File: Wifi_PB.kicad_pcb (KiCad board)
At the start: 2 copper layers, 100 x 49.7 mm, 208 parts, among them P1 CONN_01X02, P10 CONN_01X01, P12 CONN_01X04, P13 CONN_01X04, P14 CONN_01X04, P15 USB_MINI, P16 CONN_01X01, P17 CONN_01X01, P18 CONN_01X01, P19 CONN_01X01, P2 CONN_01X03, P3 CONN_01X03, P4 CONN_01X03, P5 CONN_01X03, P6 CONN_01X01, P7 CONN_01X01, P8 CONN_01X01, P9 CONN_01X01, Q1 SMBT3904, Q10 BC849, Q11 NX2301P, Q2 SMBT3904, Q3 BSS138, Q4 BSS138, Q5 SMBT3904, Q6 SMBT3904, Q7 SMBT3904, Q8 SMBT3904, Q9 SMBT3904, SW1 Pulsador_2p, SW2 Pulsador_2p, SW3 Pulsador_2p, SW4 Pulsador_2p, U1 MCP73831T, U10 Matriz_5x7_Anodo_Filas, U11 40106, U12 MCP1640, U2 LD1117S33TR, U3 CH340G, U4 ESP8266, U5 MMA7660FC, U6 MCP23017, U7 MCP23017, U8 MCP3204, U9 PCA9551, Y1 Cristal

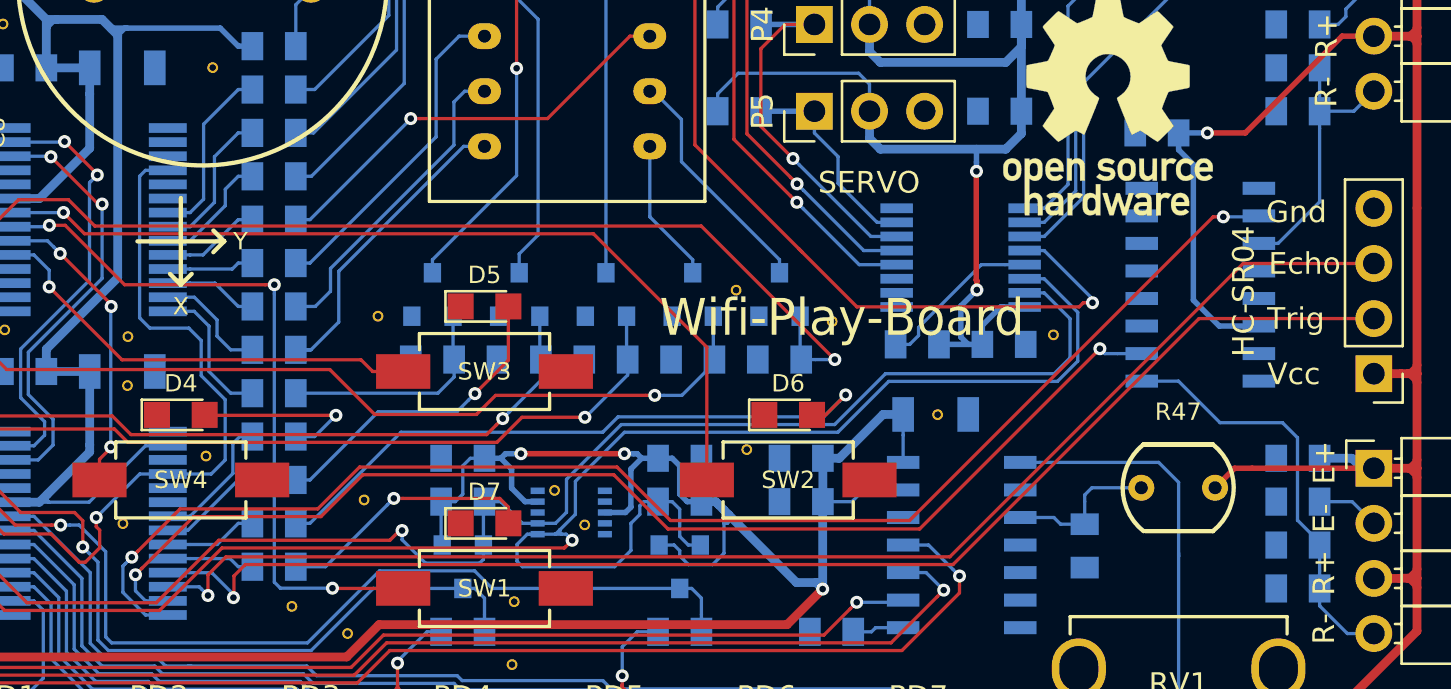
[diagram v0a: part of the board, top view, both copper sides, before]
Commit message: modificada huella de U7 a SOIC14. Corrige issue #1
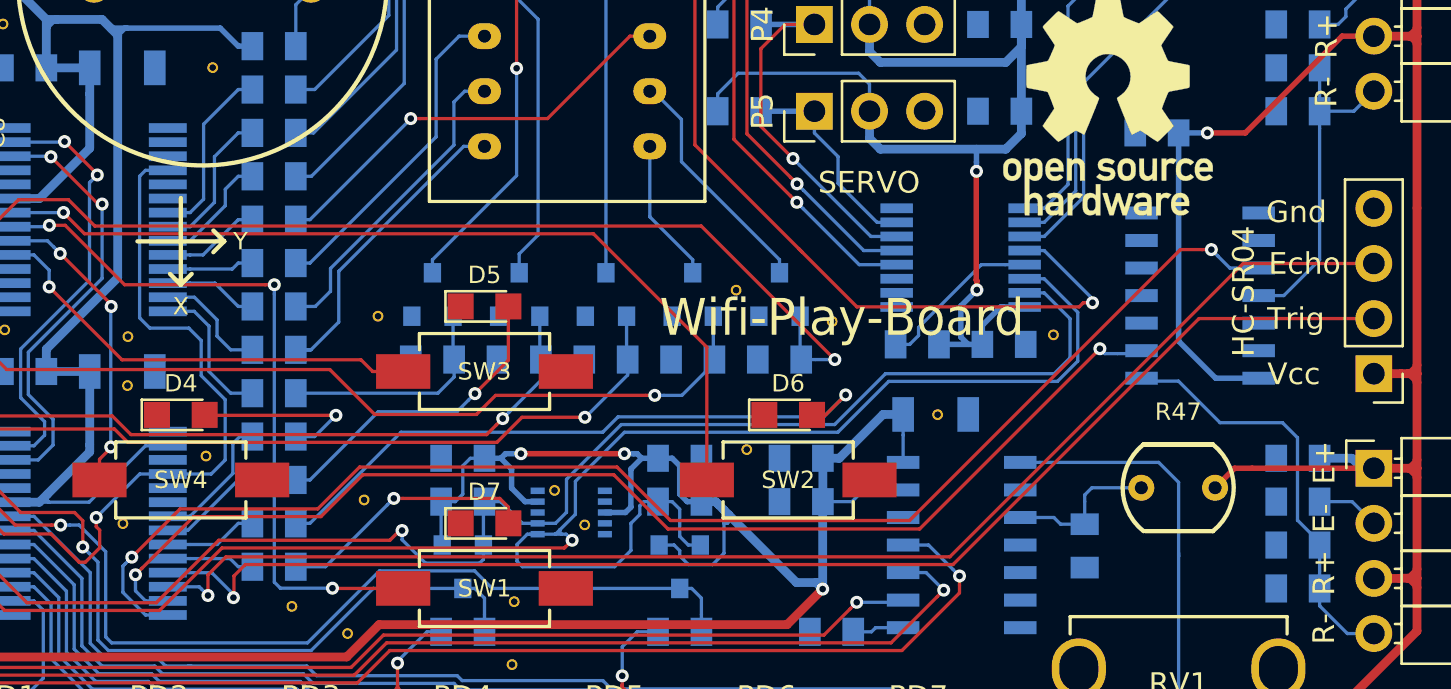
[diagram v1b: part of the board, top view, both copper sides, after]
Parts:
- C1, C14, C15, C20, C4: value 4,7u -> 4u7
- D3: value D_Schottky_ALT -> MBR0520
- R38, R62, R63, R64: value R -> 220
- U11: footprint Housings_SOIC:SOIC-16_3.9x9.9mm_Pitch1.27mm -> Housings_SOIC:SOIC-14_3.9x8.7mm_Pitch1.27mm
- moved U11 0.50 mm to (142.0, 60.5)
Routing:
- net Net-(C33-Pad1): track 12.7 -> 15.2 mm
- net +5V: track 505.8 -> 508.3 mm
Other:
- board text added: "03/17"
- board text added: "V0.1.1"
- board text removed: "02/17"
- board text removed: "V0.1"

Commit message: cambiado el driver led al PCA9634
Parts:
- removed R16: 10K, Resistencias:R_0805
- U9: value PCA9551 -> PCA9634; footprint Housings_SSOP:TSSOP-16_4.4x5mm_Pitch0.65mm -> Housings_SSOP:TSSOP-20_4.4x6.5mm_Pitch0.65mm
- moved U9 0.75 mm to (131.0, 58.0)
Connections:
- U9 pad 10: LED_BLUE -> GND
- U9 pad 11: LED_RED -> LED_GREEN
- U9 pad 12: BUZZER -> LED_BLUE
- U9 pad 13: Net-(R16-Pad2) -> LED_RED
- U9 pad 14: SCL -> BUZZER
- U9 pad 15: SDA -> GND
- U9 pad 4: SERVO1 -> GND
- U9 pad 5: SERVO2 -> GND
- U9 pad 6: SERVO3 -> SERVO1
- U9 pad 7: SERVO4 -> SERVO2
- U9 pad 8: GND -> SERVO3
- U9 pad 9: LED_GREEN -> SERVO4
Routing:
- net Net-(R16-Pad2): track 7.69 -> 0.00 mm
- net +5V: track 508.3 -> 512.3 mm
- net SERVO2: track 22.7 -> 21.3 mm
- net LED_GREEN: track 12.4 -> 11.4 mm
- net LED_BLUE: track 13.9 -> 12.9 mm
- net LED_RED: track 15.3 -> 14.4 mm
- net SERVO4: track 9.68 -> 9.09 mm
- net SERVO3: track 17.3 -> 16.7 mm
- net SERVO1: track 28.1 -> 27.5 mm
